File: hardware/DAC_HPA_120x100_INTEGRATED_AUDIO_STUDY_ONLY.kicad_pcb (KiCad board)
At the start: 4 copper layers, 120 x 100 mm, 544 parts, among them J101 GCT USB4105-GF-A, J201 PCB pads (no component), J202 PCB pads (no component), J701 G-Switch GT-3321667P-01, J702 HRO PJ-332A-6A, K601 TLP3545A, K602 TLP3545A, K603 TLP3545A, K604 TLP3545A, Q207 AO3400A, Q502 AO3400A, Q503 AO3400A, Q504 AO3400A, Q505 AO3400A, Q506 AO3400A, Q507 MMBT3904, Q612 MMBT3904, Q614 MMBT3904, Q616 AO3400A, Q617 AO3400A, Q618 2N7002, Q619 AO3400A, Q620 AO3400A, Q621 2N7002, Q622 AO3400A, Q623 MMBT3904, Q624 MMBT3904, Q625 MMBT3904, Q626 MMBT3904, Q627 MMBT3904, U101 ST USBLC6-2SC6, U102 TI TPS25200DRVR, U103 TI TPD2E2U06DRLR, U201 CH32V307RCT6, U202 AGRV2KQ32, U205 74LVC1G157, U206 74LVC1G11, U208 74LVC3G34, U301 ES9018K2M, U302 3.3 V, 250 mA, U303 1.300 V (R533/R534), U401 OPA1622IDRCR, U402 OPA1622IDRCR, U403 OPA2210IDGKR, U404 OPA2210IDGKR, U501 +3.85 / -3.72 V, U502 3.3 V, 150 mA, U503 TI TPS259621DDAR, U504 3.3 V, 1 A, U505 TI TMUX1101DBVR, U603 TLV1704, U604 OPA2333, U605 TLV3402, U606 TLV1704, U607 74AUP1G17, U608 74LVC1G74, U609 TLV1704, U610 TLV1704, U611 TLV1704, U612 TLV1704, U613 TLV3402, U614 TLV3402, U615 TLV3402, U616 TLV3402, U617 TLV3402, U618 TLV3402, U619 TLV3402, U620 TLV3402, U621 SN74AUP2G17DCKR, X201 80.000 MHz, X202 49.152 MHz, X203 45.1584 MHz, Y201 8 MHz

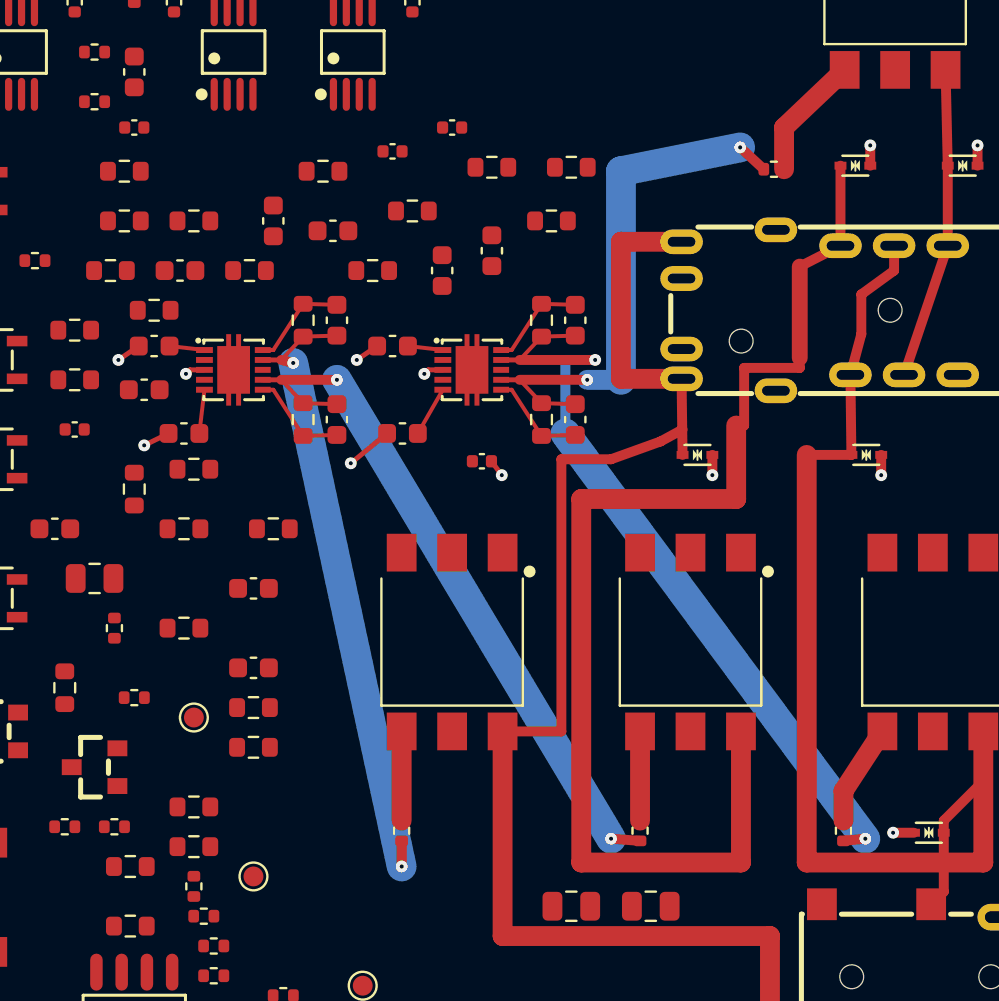
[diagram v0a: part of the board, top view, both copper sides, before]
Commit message: Route amplifier enables and audit low-DCR output-link ECO
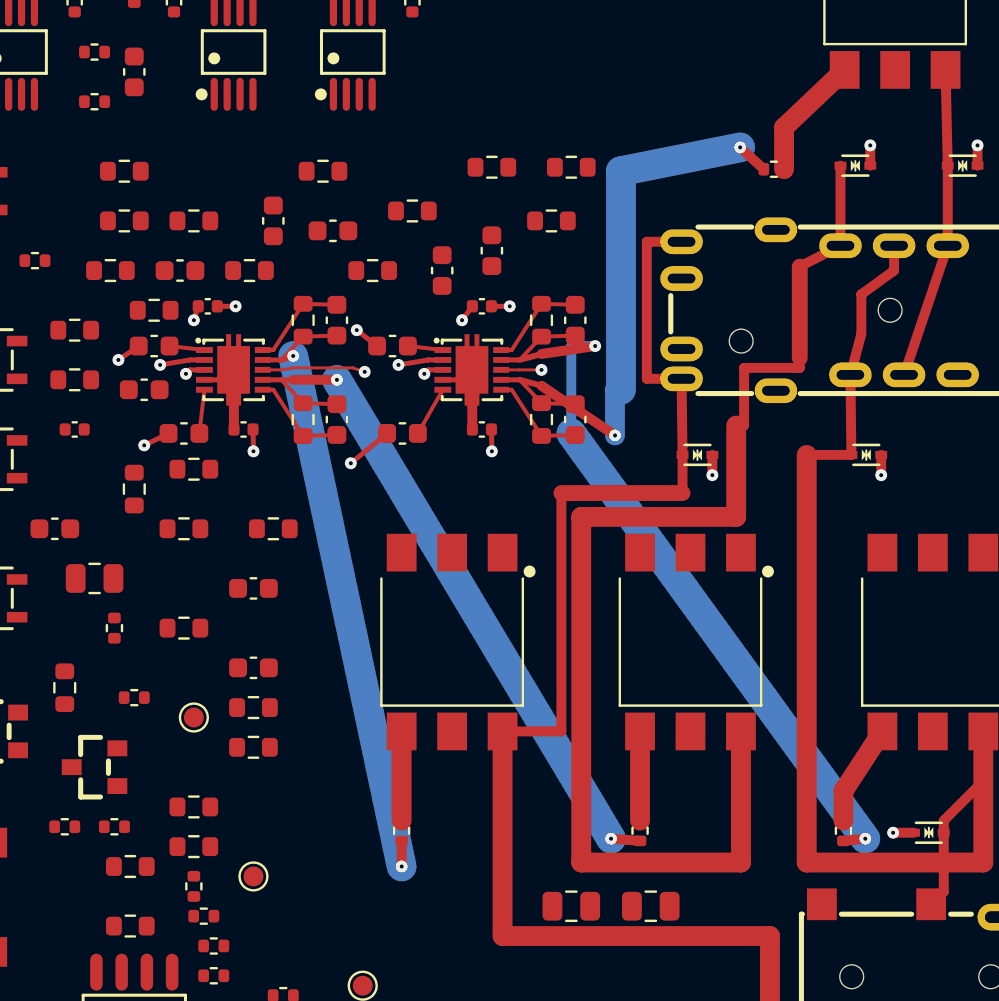
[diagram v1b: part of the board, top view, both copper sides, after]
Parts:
- moved C411 19.7 mm to (129.5, 75.8)
- moved C412 15.3 mm to (129.5, 82.0)
- moved C409 12.1 mm to (115.7, 75.8)
- moved C410 12.1 mm to (117.5, 82.0)
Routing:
- net VPOS: track 0.00 -> 51.6 mm, vias 0 -> 6
- net VNEG: track 0.00 -> 9.22 mm
- net N4_RN_OUT: track 27.6 -> 31.2 mm
- net GND: track 16.2 -> 19.4 mm, vias 14 -> 17
- net JACK_LP: track 80.1 -> 77.4 mm

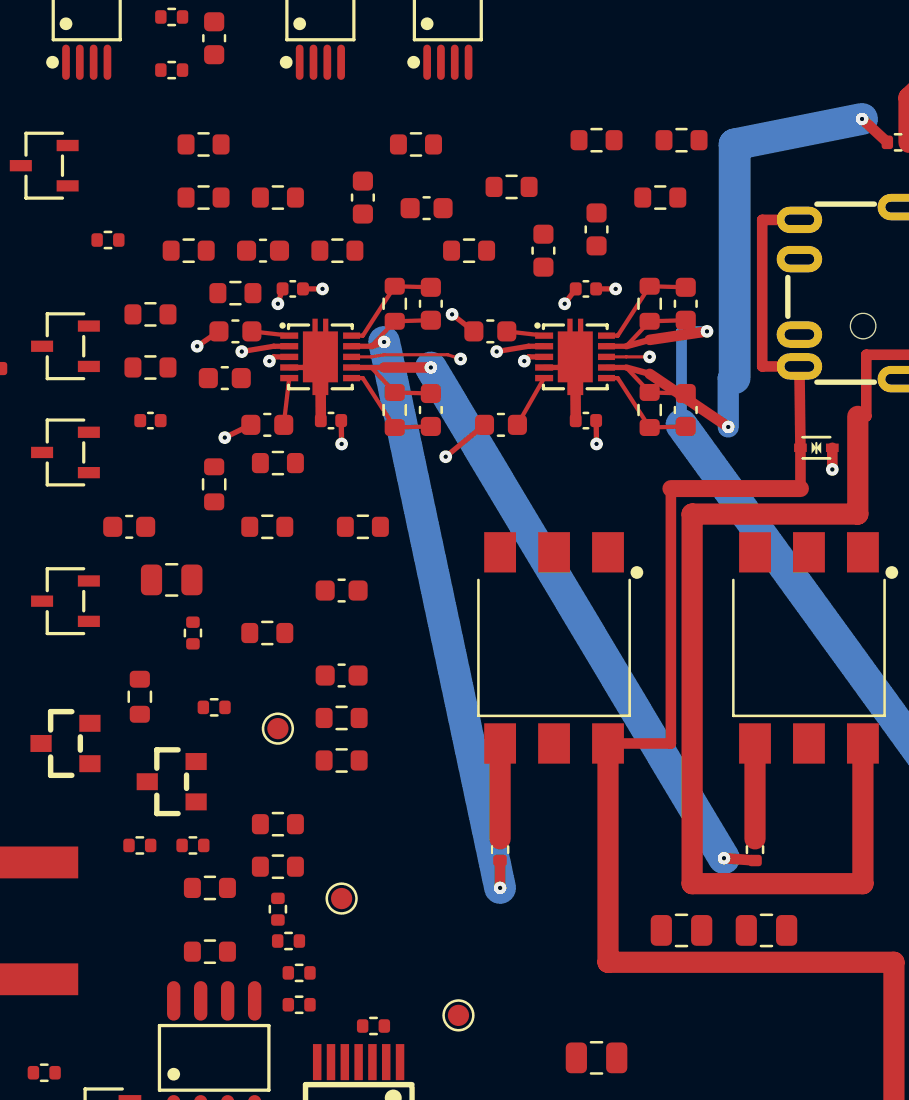
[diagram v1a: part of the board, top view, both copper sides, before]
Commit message: Manually route eight amplifier input T networks
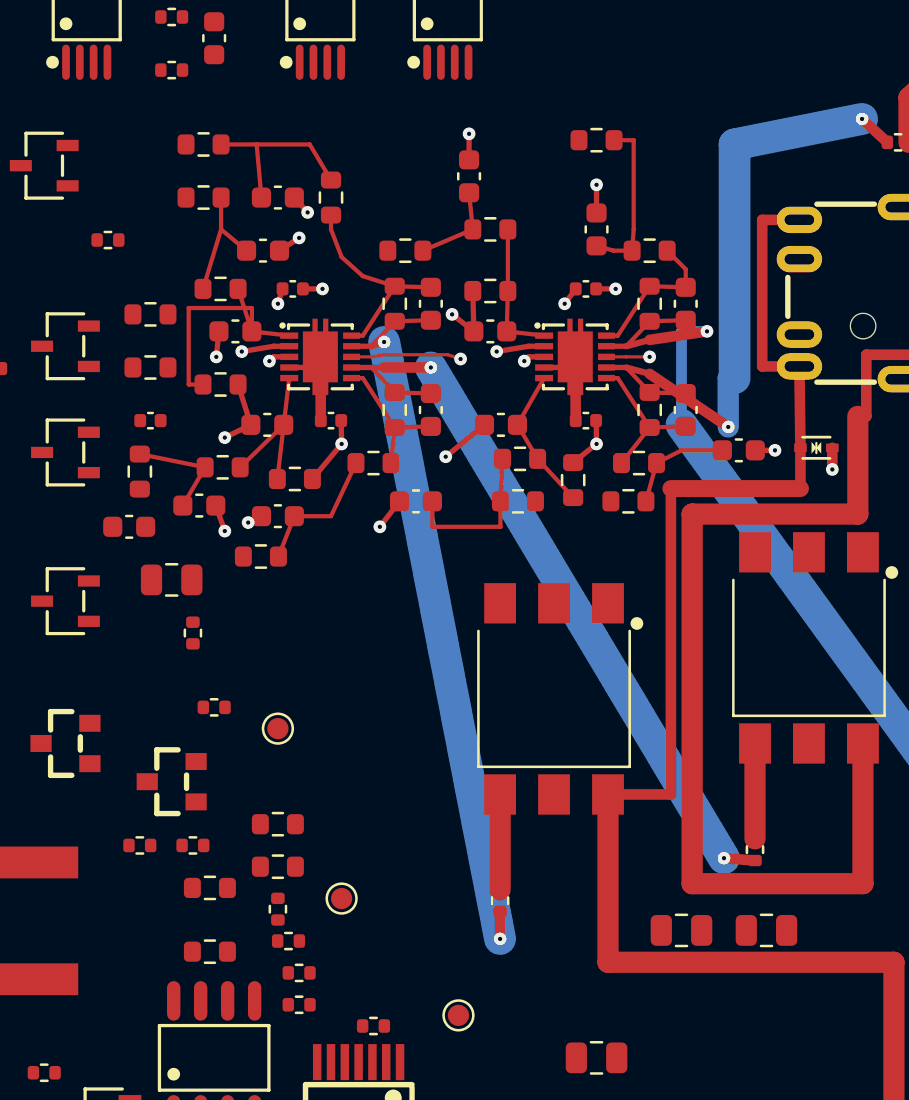
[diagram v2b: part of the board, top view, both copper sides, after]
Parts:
- moved R413 24.8 mm to (131.5, 85.8), turned to 0 degrees
- moved R443 21.7 mm to (125.0, 73.0)
- moved C437 21.5 mm to (136.7, 83.4)
- moved R405 20.7 mm to (114.2, 88.4)
- moved R442 20.2 mm to (132.5, 74.0)
- moved R445 16.5 mm to (126.4, 83.8)
- moved C433 16.1 mm to (115.0, 86.5), turned to 180 degrees
- moved R440 14.5 mm to (119.5, 84.0)
- moved R411 14.0 mm to (121.0, 74.0)
- moved R415 13.2 mm to (126.3, 85.8), turned to 180 degrees
- moved R412 12.6 mm to (125.0, 75.9), turned to 180 degrees
- moved R444 12.5 mm to (132.0, 84.0), turned to 180 degrees
- moved R416 11.9 mm to (128.9, 84.8), turned to 90 degrees
- moved R404 8.36 mm to (112.3, 80.3)
- moved R441 8.22 mm to (112.4, 84.2)
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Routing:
- net GND: track 19.4 -> 35.8 mm, vias 17 -> 25
- net N4_LP_INP: track 1.77 -> 12.2 mm
- net N4_LP_TN: track 0.00 -> 8.64 mm
- net N4_RP_TN: track 0.00 -> 7.83 mm
- net N4_RN_TP: track 0.00 -> 7.60 mm
- net N4_LN_TN: track 0.00 -> 6.53 mm
- net N4_LP_TP: track 0.00 -> 5.99 mm
- net N4_LN_INP: track 2.21 -> 7.65 mm
- net N4_LN_TP: track 0.00 -> 5.22 mm
- net N4_RN_TN: track 0.00 -> 5.11 mm
- net N4_LP_INN: track 5.00 -> 9.99 mm
- net N4_RP_INP: track 1.77 -> 6.57 mm
- net N4_RN_INP: track 2.53 -> 6.87 mm
- net N4_RP_TP: track 0.00 -> 4.29 mm
- net N4_LP_OUT: track 32.4 -> 34.8 mm
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
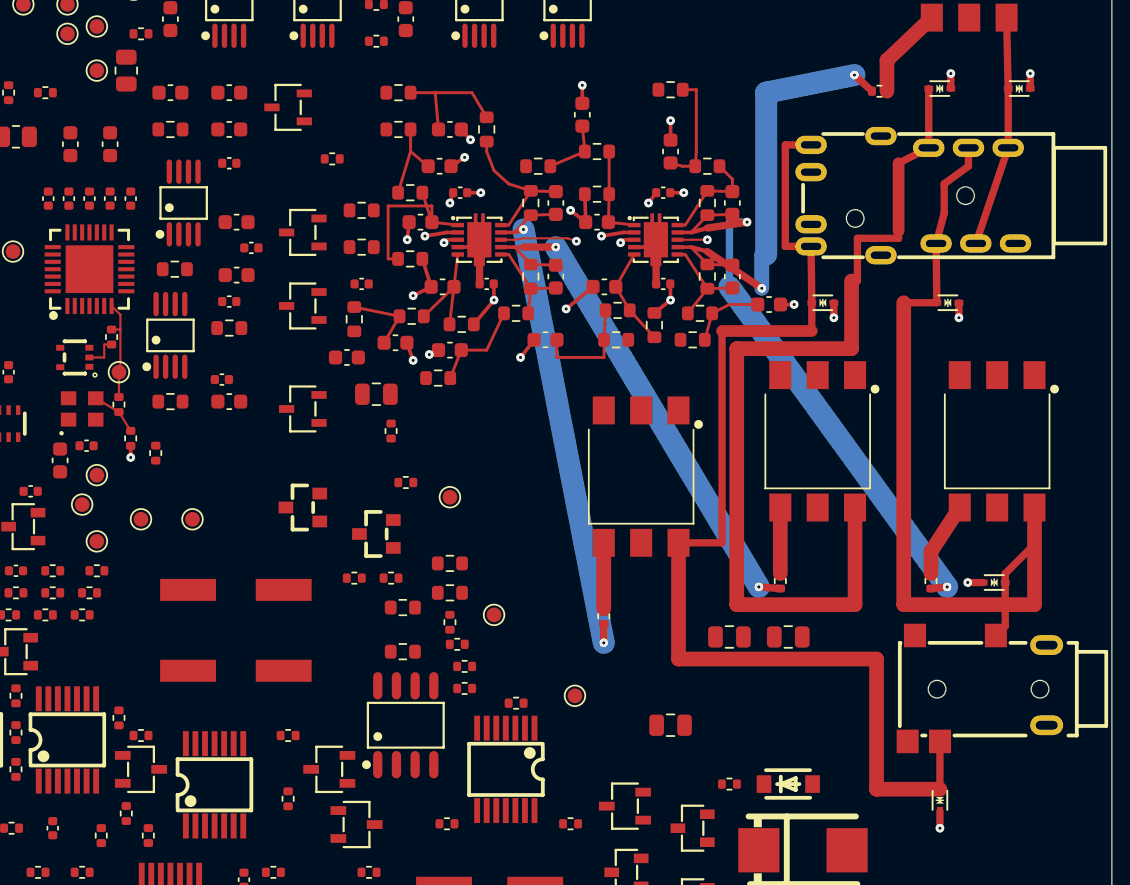
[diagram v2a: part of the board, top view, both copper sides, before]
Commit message: Replace right-angle audio bends with manual 45-degree routes
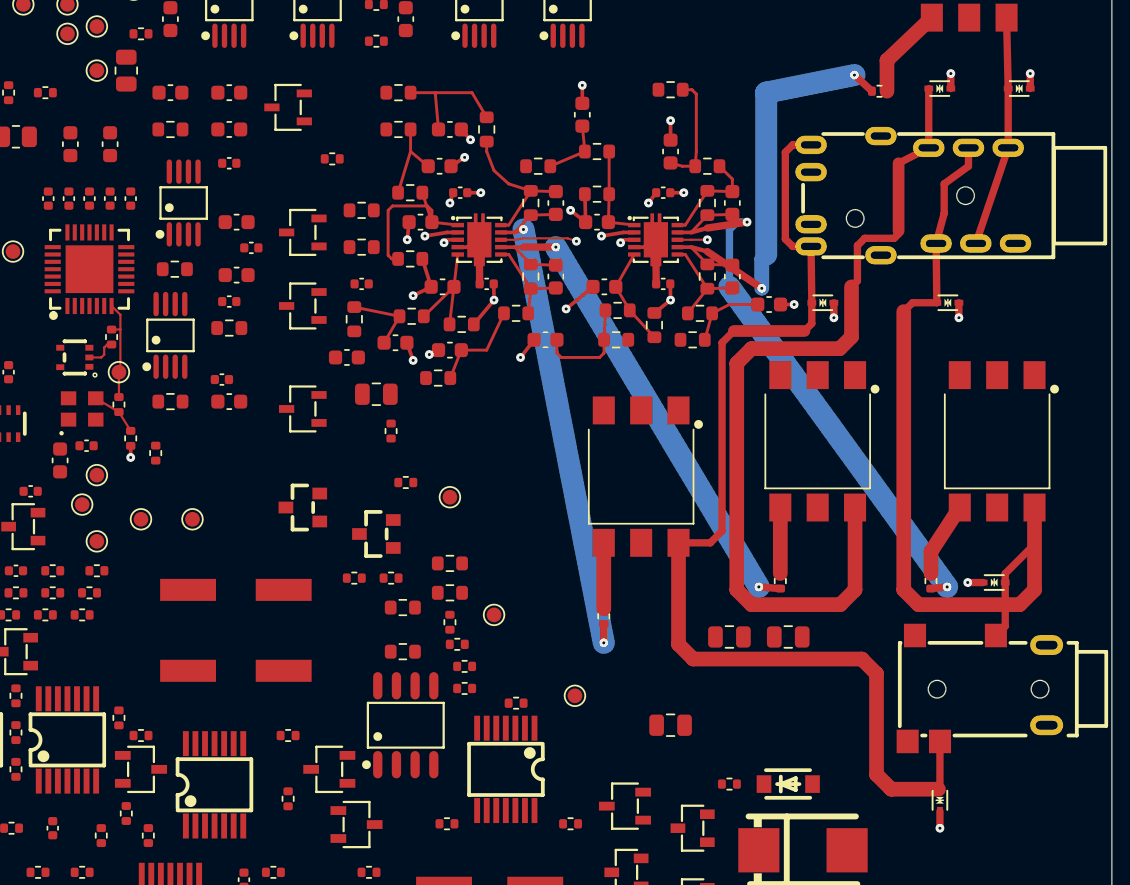
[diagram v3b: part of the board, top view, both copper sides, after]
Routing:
- net JACK_LP: track 77.4 -> 73.5 mm
- net JACK_LN: track 62.0 -> 59.0 mm
- net JACK_RP: track 59.5 -> 58.0 mm
- net VPOS: track 51.6 -> 50.6 mm

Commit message: Route manual DAC I/V and U501 macros with chamfered copper
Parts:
- moved R504 10.9 mm to (76.0, 131.6), turned to 0 degrees
- moved C424 9.92 mm to (93.8, 73.3)
- moved R501 6.80 mm to (70.0, 135.6)
- moved C421 5.64 mm to (103.7, 80.2)
- moved R503 5.49 mm to (76.0, 129.9), turned to 180 degrees
- moved R432 5.08 mm to (104.0, 78.6)
- moved R431 5.00 mm to (104.0, 76.8), turned to 180 degrees
- moved C510 5.00 mm to (68.5, 128.0)
- moved R423 5.00 mm to (101.0, 79.3), turned to -90 degrees
- moved C509 4.66 mm to (73.3, 135.8), turned to -90 degrees
- moved C419 3.83 mm to (96.3, 91.0)
- moved C425 3.80 mm to (100.0, 87.0)
- moved R502 3.75 mm to (68.3, 135.6), turned to -90 degrees
- moved D405 3.60 mm to (108.6, 78.5)
- moved C426 3.27 mm to (98.8, 85.3), turned to -90 degrees
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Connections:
- U403 pad 1: N4_IVL_P -> N4_IVL_N
- U403 pad 2: DACL -> DACLB
- U403 pad 6: DACLB -> DACL
- U403 pad 7: N4_IVL_N -> N4_IVL_P
- U404 pad 1: N4_IVR_P -> N4_IVR_N
- U404 pad 2: DACR -> DACRB
- U404 pad 6: DACRB -> DACR
- U404 pad 7: N4_IVR_N -> N4_IVR_P
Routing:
- net N4_IVR_N: track 0.00 -> 90.8 mm, vias 0 -> 5
- net N4_IVR_P: track 0.00 -> 83.6 mm, vias 0 -> 3
- net N4_IVL_N: track 0.00 -> 53.7 mm, vias 0 -> 4
- net N4_IVL_P: track 0.00 -> 47.5 mm, vias 0 -> 4
- net VREF: track 0.00 -> 37.6 mm, vias 0 -> 6
- net 3V3A: track 0.00 -> 29.5 mm, vias 0 -> 3
- net 5V_ANA_F: track 0.00 -> 25.1 mm, vias 0 -> 4
- net VPOS: track 50.6 -> 66.7 mm, vias 6 -> 8
- net GND: track 35.8 -> 51.8 mm, vias 25 -> 37
- net VNEG: track 9.22 -> 23.0 mm, vias 0 -> 2
- net DACRB: track 0.00 -> 11.8 mm
- net DACL: track 0.00 -> 11.5 mm
- net DACR: track 0.00 -> 10.8 mm
- net DACLB: track 0.00 -> 9.71 mm
- net N4_VNEG_IV: track 0.00 -> 8.70 mm, vias 0 -> 2
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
